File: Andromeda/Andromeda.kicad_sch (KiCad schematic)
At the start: 0 parts

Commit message: feat(hardware): add power management hierarchical sheet
- Introduces `Power.kicad_sch` for the main power management circuitry.
- Integrates the Nordic NPM2100-QEAA-R7 PMIC and related power components (battery, caps, inductors, resistors, switch).
- Configures the KiCad project to enable SPICE simulation and updates annotation settings.
- Instantiates the new 'Power' sheet into the top-level `Andromeda.kicad_sch`.
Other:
- added sheet Power (Power.kicad_sch)
- company: (none) -> Vion Qaro
- title: (none) -> Andromeda
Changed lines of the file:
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@@
 	(generator_version "10.0")
 	(paper "A4")
+	(title_block
+		(title "Andromeda")
+		(company "Vion Qaro")
+	)
+	(sheet
+		(at 76.2 50.8)
+		(size 25.4 27.94)
+		(exclude_from_sim no)
+		(in_bom yes)
+		(on_board yes)
+		(dnp no)
+		(fields_autoplaced yes)
+		(stroke
+			(width 0.1524)
+			(type solid)
+		)
+		(fill
+			(color 0 0 0 0)
+		)
+		(property "Sheetname" "Power"
+			(at 76.2 50.0884 0)
+			(show_name no)
+			(do_not_autoplace no)
+			(effects
+				(font
+					(size 1.27 1.27)
+				)
+				(justify left bottom)
+			)
+		)
+		(property "Sheetfile" "Power.kicad_sch"
+			(at 76.2 79.3246 0)
+			(show_name no)
+			(do_not_autoplace no)
+			(effects
+				(font
+					(size 1.27 1.27)
+				)
+				(justify left top)
+			)
+		)
+		(pin "PMIC_GPIO0" bidirectional
+			(at 101.6 73.66 0)
+			(effects
+				(font
+					(size 1.27 1.27)
+				)
+				(justify right)
+			)
+		)
+		(pin "PMIC_GPIO1" bidirectional
+			(at 101.6 76.2 0)
+			(effects
+				(font
+					(size 1.27 1.27)
+				)
+				(justify right)
+			)
+		)
+		(pin "PMIC_PG_RESET" bidirectional
+			(at 101.6 68.58 0)
+			(effects
+				(font
+					(size 1.27 1.27)
+				)
+				(justify right)
+			)
+		)
+		(pin "PMIC_SCL" input
+			(at 101.6 63.5 0)
+			(effects
+				(font
+					(size 1.27 1.27)
+				)
+				(justify right)
+			)
+		)
+		(pin "PMIC_SDA" bidirectional
+			(at 101.6 60.96 0)
+			(effects
+				(font
+					(size 1.27 1.27)
+				)
+				(justify right)
+			)
+		)
+		(pin "PMIC_VOUTLDO" output
+			(at 101.6 53.34 0)
+			(effects
+				(font
+					(size 1.27 1.27)
+				)
+				(justify right)
+			)
+		)
+		(instances
+			(project "Andromeda"
+				(path "/f75d7f4e-9b64-477b-ae26-656ea39c557c"
+					(page "2")
+				)
+			)
+		)
+	)
 	(sheet_instances
 		(path "/"

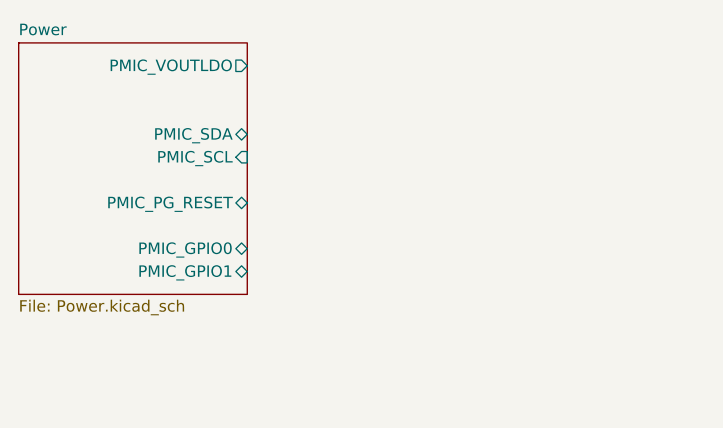
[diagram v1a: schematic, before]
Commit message: feat(hardware): add Host hierarchical schematic sheet
- Introduces `Host.kicad_sch` as a new hierarchical sheet for host interface circuitry.
- Instantiates the new 'Host' sheet into the top-level `Andromeda.kicad_sch`.
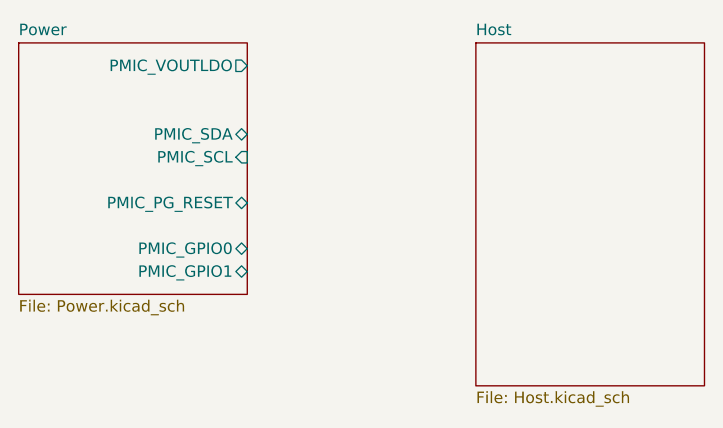
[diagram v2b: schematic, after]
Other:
- added sheet Host (Host.kicad_sch)
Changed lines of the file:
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@@
+		)
+	)
+	(sheet
+		(at 127 50.8)
+		(size 25.4 38.1)
+		(exclude_from_sim no)
+		(in_bom yes)
+		(on_board yes)
+		(dnp no)
+		(fields_autoplaced yes)
+		(stroke
+			(width 0.1524)
+			(type solid)
+		)
+		(fill
+			(color 0 0 0 0)
+		)
+		(property "Sheetname" "Host"
+			(at 127 50.0884 0)
+			(show_name no)
+			(do_not_autoplace no)
+			(effects
+				(font
+					(size 1.27 1.27)
+				)
+				(justify left bottom)
+			)
+		)
+		(property "Sheetfile" "Host.kicad_sch"
+			(at 127 89.4846 0)
+			(show_name no)
+			(do_not_autoplace no)
+			(effects
+				(font
+					(size 1.27 1.27)
+				)
+				(justify left top)
+			)
+		)
+		(instances
+			(project "Andromeda"
+				(path "/f75d7f4e-9b64-477b-ae26-656ea39c557c"
+					(page "3")
+				)
+			)
 		)
 	)
